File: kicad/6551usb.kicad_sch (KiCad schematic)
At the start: 41 parts, among them J1 Conn_01x03_Male, P1 DLP-USB245R, SW1 SW_DIP_x06, U1 74LS04, U10 74LS74, U11 74LS86, U12 74LS33, U13 74LS273, U14 74LS374, U15 74LS244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

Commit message: Updated sheet titles and added screenshot
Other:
- title: (none) -> CoCo USB Serial
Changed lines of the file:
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@@
 (kicad_sch (version 20211123) (generator eeschema)
   (paper "USLedger")
+  (title_block
+    (title "CoCo USB Serial")
+    (date "2022-10-20")
+    (rev "1.0")
+  )
   (junction (at 31.75 66.04) (diameter 0) (color 0 0 0 0)
   )

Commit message: Update to 1.01
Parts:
- U7: value 74LS09 -> 74LS08; footprint Package_DIP:DIP-20_W7.62mm -> Package_DIP:DIP-14_W7.62mm
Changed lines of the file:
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@@
   (title_block
     (title "CoCo USB Serial")
-    (date "2022-10-20")
-    (rev "1.0")
+    (date "2022-11-15")
+    (rev "1.01")
   )
   (junction (at 31.75 66.04) (diameter 0) (color 0 0 0 0)
@@
       (effects (font (size 1.27 1.27)) (justify left))
     )
-    (property "Value" "74LS09" (id 1) (at 369.57 85.0899 0)
+    (property "Value" "74LS08" (id 1) (at 369.57 85.0899 0)
       (effects (font (size 1.27 1.27)) (justify left))
     )
-    (property "Footprint" "Package_DIP:DIP-20_W7.62mm" (id 2) (at 363.22 83.82 0)
+    (property "Footprint" "Package_DIP:DIP-14_W7.62mm" (id 2) (at 363.22 83.82 0)
       (effects (font (size 1.27 1.27)) hide)
     )
@@
     (in_bom yes) (on_board yes) (fields_autoplaced)
     (property "Reference" "U7" (id 0) (at 215.9 20.32 0))
-    (property "Value" "74LS09" (id 1) (at 215.9 22.86 0))
-    (property "Footprint" "Package_DIP:DIP-20_W7.62mm" (id 2) (at 215.9 29.21 0)
+    (property "Value" "74LS08" (id 1) (at 215.9 22.86 0))
+    (property "Footprint" "Package_DIP:DIP-14_W7.62mm" (id 2) (at 215.9 29.21 0)
       (effects (font (size 1.27 1.27)) hide)
     )
@@
     (in_bom yes) (on_board yes) (fields_autoplaced)
     (property "Reference" "U7" (id 0) (at 72.39 193.04 0))
-    (property "Value" "74LS09" (id 1) (at 72.39 195.58 0))
-    (property "Footprint" "Package_DIP:DIP-20_W7.62mm" (id 2) (at 72.39 201.93 0)
+    (property "Value" "74LS08" (id 1) (at 72.39 195.58 0))
+    (property "Footprint" "Package_DIP:DIP-14_W7.62mm" (id 2) (at 72.39 201.93 0)
       (effects (font (size 1.27 1.27)) hide)
     )
@@
     (in_bom yes) (on_board yes) (fields_autoplaced)
     (property "Reference" "U7" (id 0) (at 217.17 71.12 0))
-    (property "Value" "74LS09" (id 1) (at 217.17 73.66 0))
-    (property "Footprint" "Package_DIP:DIP-20_W7.62mm" (id 2) (at 217.17 80.01 0)
+    (property "Value" "74LS08" (id 1) (at 217.17 73.66 0))
+    (property "Footprint" "Package_DIP:DIP-14_W7.62mm" (id 2) (at 217.17 80.01 0)
       (effects (font (size 1.27 1.27)) hide)
     )
@@
     (in_bom yes) (on_board yes) (fields_autoplaced)
     (property "Reference" "U7" (id 0) (at 223.52 153.67 0))
-    (property "Value" "74LS09" (id 1) (at 223.52 156.21 0))
-    (property "Footprint" "Package_DIP:DIP-20_W7.62mm" (id 2) (at 223.52 162.56 0)
+    (property "Value" "74LS08" (id 1) (at 223.52 156.21 0))
+    (property "Footprint" "Package_DIP:DIP-14_W7.62mm" (id 2) (at 223.52 162.56 0)
       (effects (font (size 1.27 1.27)) hide)
     )
@@
     )
     (path "/5c4b6a91-b6b3-4d33-8f16-491e598c7609"
-      (reference "U7") (unit 1) (value "74LS09") (footprint "Package_DIP:DIP-20_W7.62mm")
+      (reference "U7") (unit 1) (value "74LS08") (footprint "Package_DIP:DIP-14_W7.62mm")
     )
     (path "/6f7cd65b-8a3f-44c9-a30b-45360deb423b"
-      (reference "U7") (unit 2) (value "74LS09") (footprint "Package_DIP:DIP-20_W7.62mm")
+      (reference "U7") (unit 2) (value "74LS08") (footprint "Package_DIP:DIP-14_W7.62mm")
     )
     (path "/c10ba5b8-3761-490f-afbf-4051e9165c4f"
-      (reference "U7") (unit 3) (value "74LS09") (footprint "Package_DIP:DIP-20_W7.62mm")
+      (reference "U7") (unit 3) (value "74LS08") (footprint "Package_DIP:DIP-14_W7.62mm")
     )
     (path "/44462aa4-01e8-4015-b584-92461e061d7f"
-      (reference "U7") (unit 4) (value "74LS09") (footprint "Package_DIP:DIP-20_W7.62mm")
+      (reference "U7") (unit 4) (value "74LS08") (footprint "Package_DIP:DIP-14_W7.62mm")
     )
     (path "/2711488f-b584-4b80-8142-09d25e72acd8"
-      (reference "U7") (unit 5) (value "74LS09") (footprint "Package_DIP:DIP-20_W7.62mm")
+      (reference "U7") (unit 5) (value "74LS08") (footprint "Package_DIP:DIP-14_W7.62mm")
     )
     (path "/37e1bdad-930c-4338-b37c-a4cfc274b35f"

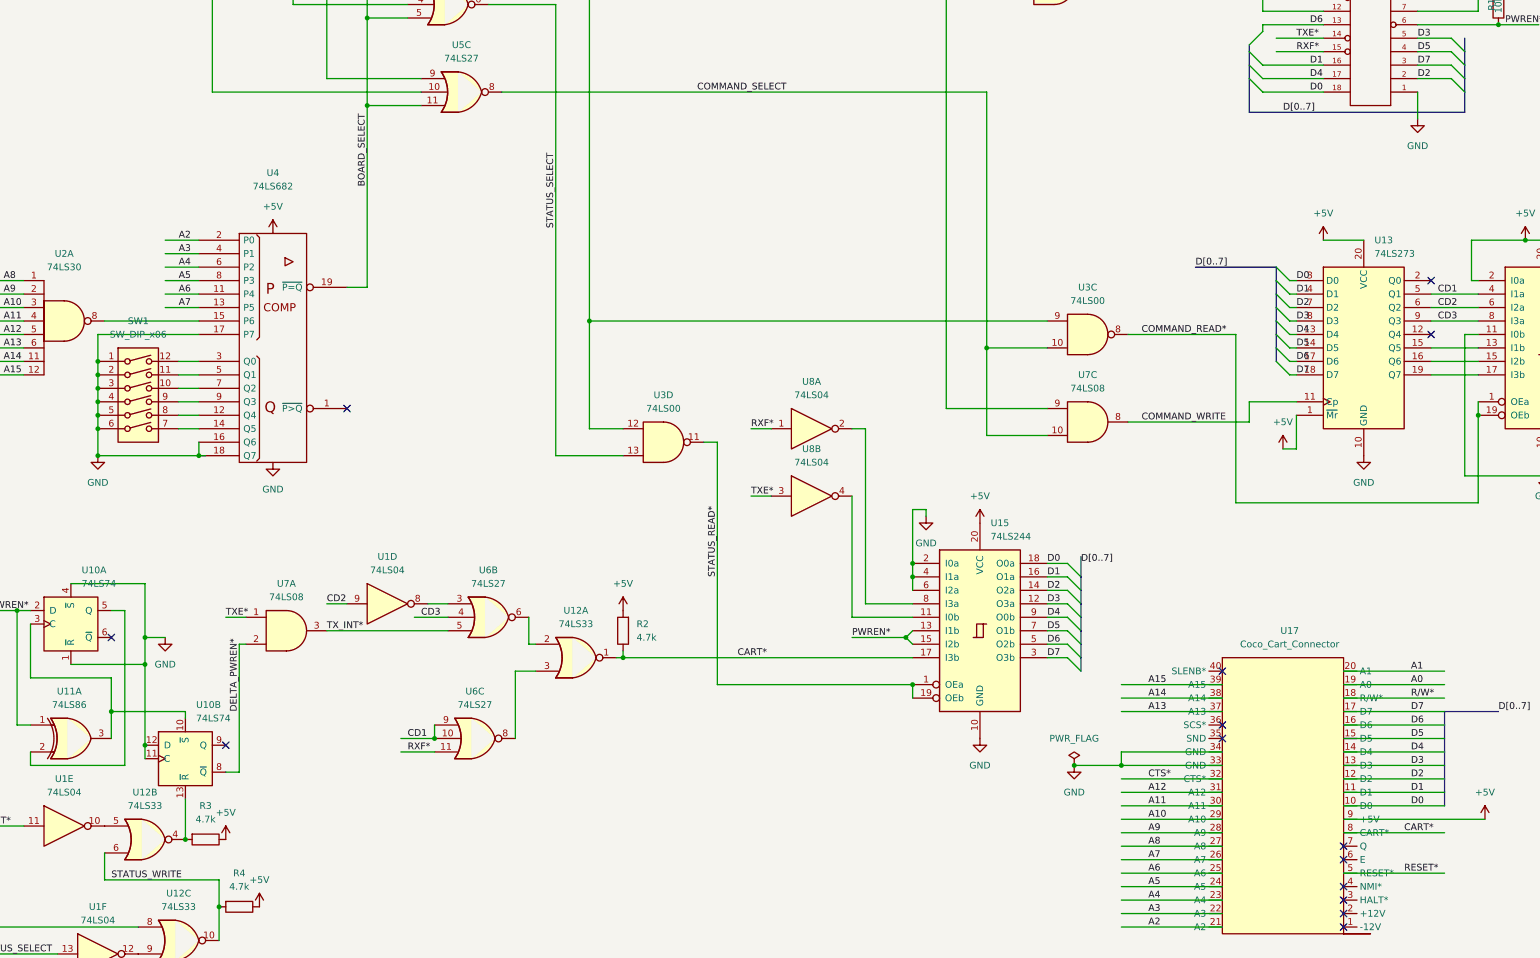
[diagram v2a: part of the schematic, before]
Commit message: Updated to 1.02 to fix E line
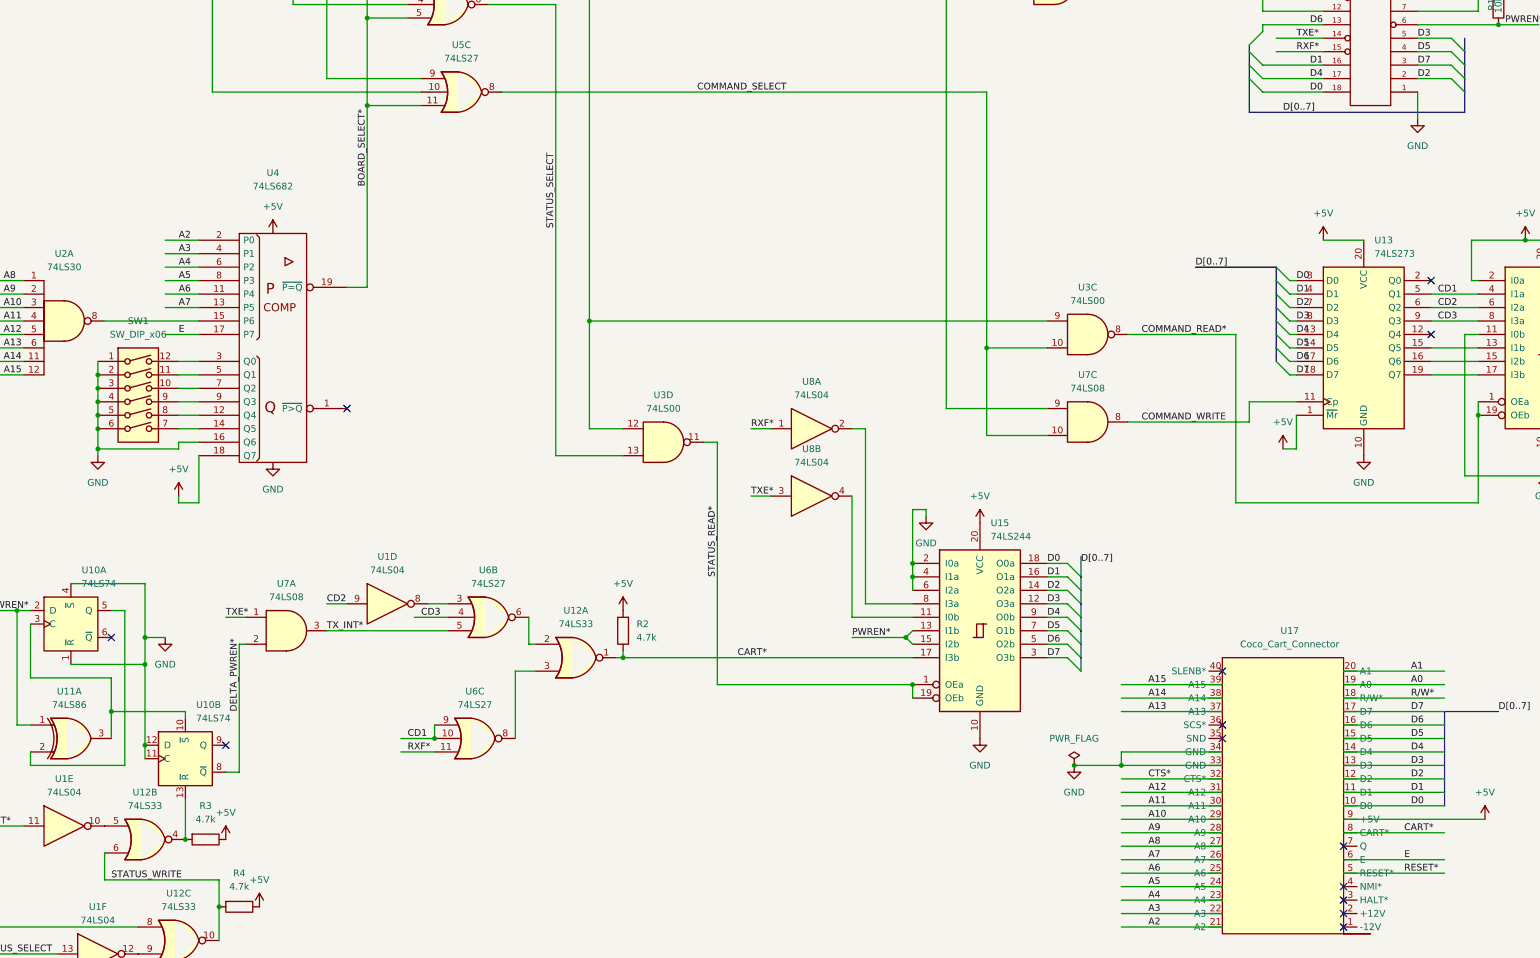
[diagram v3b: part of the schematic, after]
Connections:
- net +5V: now also U4.18 (Q7)
- net GND: no longer U4.17 (P7), U4.18 (Q7)
- net E: now reaches U17.6 (E)
- net E: now also U4.17 (P7)
- net BOARD_SELECT renamed BOARD_SELECT*
- no-connect marks 23 -> 22
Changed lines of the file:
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@@
   (title_block
     (title "CoCo USB Serial")
-    (date "2022-11-15")
-    (rev "1.01")
+    (date "2022-11-23")
+    (rev "1.02")
   )
   (junction (at 31.75 66.04) (diameter 0) (color 0 0 0 0)
@@
   (junction (at 406.4 209.55) (diameter 0) (color 0 0 0 0)
   )
-  (junction (at 36.83 151.13) (diameter 0) (color 0 0 0 0)
-  )
   (junction (at 346.71 33.02) (diameter 0) (color 0 0 0 0)
   )
@@
   (junction (at 190.5 212.09) (diameter 0) (color 0 0 0 0)
   )
+  (junction (at 36.83 167.64) (diameter 0) (color 0 0 0 0)
+  )
   (junction (at 208.28 34.29) (diameter 0) (color 0 0 0 0)
   )
@@
   (junction (at 398.78 220.98) (diameter 0) (color 0 0 0 0)
   )
-  (junction (at 55.88 168.91) (diameter 0) (color 0 0 0 0)
-  )
   (junction (at 354.33 209.55) (diameter 0) (color 0 0 0 0)
   )
@@
   (junction (at 345.44 217.17) (diameter 0) (color 0 0 0 0)
   )
-  (junction (at 36.83 168.91) (diameter 0) (color 0 0 0 0)
-  )
   (junction (at 36.83 158.75) (diameter 0) (color 0 0 0 0)
   )
@@
   (no_connect (at 248.92 209.55))
   (no_connect (at 271.78 242.57))
-  (no_connect (at 271.78 245.11))
   (no_connect (at 271.78 250.19))
   (no_connect (at 271.78 252.73))
@@
     (stroke (width 0) (type default) (color 0 0 0 0))
   )
+  (wire (pts (xy 52.07 176.53) (xy 52.07 177.8))
+    (stroke (width 0) (type default) (color 0 0 0 0))
+  )
   (wire (pts (xy 398.78 217.17) (xy 406.4 217.17))
     (stroke (width 0) (type default) (color 0 0 0 0))
@@
     (stroke (width 0) (type default) (color 0 0 0 0))
   )
-  (wire (pts (xy 36.83 163.83) (xy 36.83 168.91))
+  (wire (pts (xy 36.83 163.83) (xy 36.83 167.64))
     (stroke (width 0) (type default) (color 0 0 0 0))
   )
@@
     (stroke (width 0) (type default) (color 0 0 0 0))
   )
+  (wire (pts (xy 55.88 177.8) (xy 52.07 177.8))
+    (stroke (width 0) (type default) (color 0 0 0 0))
+  )
   (wire (pts (xy 261.62 146.05) (xy 262.89 146.05))
     (stroke (width 0) (type default) (color 0 0 0 0))
@@
     (stroke (width 0) (type default) (color 0 0 0 0))
   )
-  (wire (pts (xy 55.88 146.05) (xy 36.83 146.05))
-    (stroke (width 0) (type default) (color 0 0 0 0))
-  )
   (wire (pts (xy 105.41 53.34) (xy 73.66 53.34))
     (stroke (width 0) (type default) (color 0 0 0 0))
@@
     (stroke (width 0) (type default) (color 0 0 0 0))
   )
+  (wire (pts (xy 271.78 245.11) (xy 290.83 245.11))
+    (stroke (width 0) (type default) (color 0 0 0 0))
+  )
   (wire (pts (xy 229.87 212.09) (xy 248.92 212.09))
     (stroke (width 0) (type default) (color 0 0 0 0))
@@
     (stroke (width 0) (type default) (color 0 0 0 0))
   )
-  (wire (pts (xy 55.88 166.37) (xy 55.88 168.91))
-    (stroke (width 0) (type default) (color 0 0 0 0))
-  )
   (bus (pts (xy 222.25 199.39) (xy 222.25 201.93))
     (stroke (width 0) (type default) (color 0 0 0 0))
@@
     (stroke (width 0) (type default) (color 0 0 0 0))
   )
+  (wire (pts (xy 55.88 166.37) (xy 52.07 166.37))
+    (stroke (width 0) (type default) (color 0 0 0 0))
+  )
   (wire (pts (xy 229.87 232.41) (xy 248.92 232.41))
     (stroke (width 0) (type default) (color 0 0 0 0))
@@
     (stroke (width 0) (type default) (color 0 0 0 0))
   )
-  (wire (pts (xy 57.15 168.91) (xy 55.88 168.91))
-    (stroke (width 0) (type default) (color 0 0 0 0))
-  )
   (wire (pts (xy 38.1 243.84) (xy 38.1 248.92))
     (stroke (width 0) (type default) (color 0 0 0 0))
@@
     (stroke (width 0) (type default) (color 0 0 0 0))
   )
+  (wire (pts (xy 36.83 167.64) (xy 52.07 167.64))
+    (stroke (width 0) (type default) (color 0 0 0 0))
+  )
   (wire (pts (xy 297.18 82.55) (xy 297.18 80.01))
     (stroke (width 0) (type default) (color 0 0 0 0))
@@
     (stroke (width 0) (type default) (color 0 0 0 0))
   )
-  (wire (pts (xy 55.88 168.91) (xy 36.83 168.91))
-    (stroke (width 0) (type default) (color 0 0 0 0))
-  )
   (wire (pts (xy 229.87 247.65) (xy 248.92 247.65))
     (stroke (width 0) (type default) (color 0 0 0 0))
@@
     (stroke (width 0) (type default) (color 0 0 0 0))
   )
+  (wire (pts (xy 55.88 168.91) (xy 55.88 177.8))
+    (stroke (width 0) (type default) (color 0 0 0 0))
+  )
   (wire (pts (xy 16.51 143.51) (xy 22.86 143.51))
     (stroke (width 0) (type default) (color 0 0 0 0))
@@
     (stroke (width 0) (type default) (color 0 0 0 0))
   )
+  (wire (pts (xy 52.07 166.37) (xy 52.07 167.64))
+    (stroke (width 0) (type default) (color 0 0 0 0))
+  )
   (wire (pts (xy 375.92 100.33) (xy 382.27 100.33))
     (stroke (width 0) (type default) (color 0 0 0 0))
@@
     (stroke (width 0) (type default) (color 0 0 0 0))
   )
-  (wire (pts (xy 36.83 146.05) (xy 36.83 151.13))
-    (stroke (width 0) (type default) (color 0 0 0 0))
-  )
   (bus (pts (xy 259.08 138.43) (xy 259.08 140.97))
     (stroke (width 0) (type default) (color 0 0 0 0))
@@
     (stroke (width 0) (type default) (color 0 0 0 0))
   )
+  (wire (pts (xy 49.53 146.05) (xy 55.88 146.05))
+    (stroke (width 0) (type default) (color 0 0 0 0))
+  )
   (wire (pts (xy 363.22 182.88) (xy 367.03 182.88))
     (stroke (width 0) (type default) (color 0 0 0 0))
@@
     (stroke (width 0) (type default) (color 0 0 0 0))
   )
+  (wire (pts (xy 36.83 167.64) (xy 36.83 168.91))
+    (stroke (width 0) (type default) (color 0 0 0 0))
+  )
   (wire (pts (xy 345.44 209.55) (xy 354.33 209.55))
     (stroke (width 0) (type default) (color 0 0 0 0))
@@
     (effects (font (size 1.27 1.27)) (justify left bottom))
   )
+  (label "E" (at 283.21 245.11 0)
+    (effects (font (size 1.27 1.27)) (justify left bottom))
+  )
   (label "D4" (at 262.89 146.05 0)
     (effects (font (size 1.27 1.27)) (justify left bottom))
@@
     (effects (font (size 1.27 1.27)) (justify left bottom))
   )
+  (label "E" (at 52.07 146.05 0)
+    (effects (font (size 1.27 1.27)) (justify left bottom))
+  )
   (label "D7" (at 285.75 95.25 0)
     (effects (font (size 1.27 1.27)) (justify left bottom))
@@
     (effects (font (size 1.27 1.27)) (justify left bottom))
   )
-  (label "BOARD_SELECT" (at 87.63 118.11 90)
+  (label "BOARD_SELECT*" (at 87.63 118.11 90)
     (effects (font (size 1.27 1.27)) (justify left bottom))
   )
@@
     (pin "1")
   )
+  (symbol (lib_id "power:+5V") (at 52.07 176.53 0) (unit 1)
+    (in_bom yes) (on_board yes)
+    (property "Reference" "#PWR0129" (id 0) (at 52.07 180.34 0)
+      (effects (font (size 1.27 1.27)) hide)
+    )
+    (property "Value" "+5V" (id 1) (at 52.07 171.45 0))
+    (property "Footprint" "" (id 2) (at 52.07 176.53 0)
+      (effects (font (size 1.27 1.27)) hide)
+    )
+    (property "Datasheet" "" (id 3) (at 52.07 176.53 0)
+      (effects (font (size 1.27 1.27)) hide)
+    )
+    (pin "1")
+  )
   (symbol (lib_id "power:+5V") (at 203.2 181.61 0) (unit 1)
     (in_bom yes) (on_board yes) (fields_autoplaced)
@@
       (reference "#PWR0128") (unit 1) (value "+5V") (footprint "")
     )
+    (path "/de08691b-f1d9-49e3-ae33-baaa2dbcf0ec"
+      (reference "#PWR0129") (unit 1) (value "+5V") (footprint "")
+    )
     (path "/92900cd0-548c-482b-a1b2-9ce27355b8a5"
